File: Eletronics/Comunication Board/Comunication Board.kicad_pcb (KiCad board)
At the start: 2 copper layers, 28 parts, among them K1 RELE, T1 AMS1117/3V3, U1 ESP32-S3-WROOM-1-N8R2, U2 BATERIA, U3 MAX17048G

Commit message: Comunication Board edit
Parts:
- added C10: 1 uF, Capacitor_SMD:C_0603_1608Metric, F.Cu at (158.1, 111.9)
- added C9: 1 uF, Capacitor_SMD:C_0603_1608Metric, F.Cu at (164.6, 102.2)
- added D1: 1N4007, Diode_SMD:D_SMA, F.Cu at (152.1, 110.8)
- added J1: USB, Connector_USB:USB_Micro-B_Amphenol_10118194_Horizontal, F.Cu at (153.0, 104.1)
- added J3: Conn_01x03_Female, Connector_PinSocket_2.54mm:PinSocket_1x03_P2.54mm_Vertical, F.Cu at (160.3, 103.3)
- added R10: 100 Ω, Resistor_SMD:R_0603_1608Metric, F.Cu at (164.6, 107.3)
- added R9: 100 Ω, Resistor_SMD:R_0603_1608Metric, F.Cu at (164.6, 104.7)
- moved BOOT1 6.30 mm to (186.2, 75.9)
- moved C2 6.30 mm to (210.7, 64.8)
- moved C4 6.30 mm to (202.7, 69.9)
- moved C5 6.30 mm to (201.4, 72.5)
- moved C8 6.30 mm to (195.8, 79.0)
- moved EN1 6.30 mm to (196.0, 58.8)
- moved L2 6.30 mm to (193.4, 71.4)
- moved L3 6.30 mm to (193.4, 74.0)
- moved L4 6.30 mm to (202.7, 64.9)
- moved POWER1 6.30 mm to (171.5, 74.9)
- moved R4 6.30 mm to (193.3, 76.5)
- moved R6 6.30 mm to (216.6, 57.0)
- moved R7 6.30 mm to (206.7, 64.8)
- moved R8 6.30 mm to (191.8, 80.1)
- moved U2 6.30 mm to (204.7, 59.2)
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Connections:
- K1 pad NC: GPIO -> GPIO45
- R1 pad 1: GPIO -> GPIO6
- R5 pad 1: GPIO -> GPIO5
- R6 pad 1: GPIO -> GPIO7
- U1 pad 13: unconnected-(U1-Pad13) -> USB_D-
- U1 pad 14: unconnected-(U1-Pad14) -> USB_D+
- U1 pad 18: unconnected-(U1-Pad18) -> SPI_CS
- U1 pad 19: unconnected-(U1-Pad19) -> SPI_MOSI
- U1 pad 20: unconnected-(U1-Pad20) -> SPI_CLK
- U1 pad 21: unconnected-(U1-Pad21) -> SPI_MISO
- U1 pad 26: unconnected-(U1-Pad26) -> GPIO45
- U1 pad 33: unconnected-(U1-Pad33) -> GPIO40
- U1 pad 35: unconnected-(U1-Pad35) -> GPIO42
- U1 pad 36: unconnected-(U1-Pad36) -> RXD0
- U1 pad 37: unconnected-(U1-Pad37) -> TXD0
- U1 pad 5: unconnected-(U1-Pad5) -> GPIO5
- U1 pad 6: unconnected-(U1-Pad6) -> GPIO6
- U1 pad 7: unconnected-(U1-Pad7) -> GPIO7
- U3 pad 5: AnyGPIO -> GPIO40

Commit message: Comunication board
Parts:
- added BZ1: Buzzer, Buzzer_Beeper:Buzzer_12x9.5RM7.6, F.Cu at (135.2, 52.3)
- added H4: MountingHole, SirBoardLibrary:MountingHole_M2.5_SirBoard, F.Cu at (156.9, 48.5)
- added H4: MountingHole, SirBoardLibrary:MountingHole_M2.5_SirBoard, F.Cu at (117.8, 48.5)
- added H4: MountingHole, SirBoardLibrary:MountingHole_M2.5_SirBoard, F.Cu at (156.9, 87.8)
- added H4: MountingHole, SirBoardLibrary:MountingHole_M2.5_SirBoard, F.Cu at (117.6, 87.8)
- added J2: Conn_01x04_Female, Connector_PinSocket_2.54mm:PinSocket_1x04_P2.54mm_Vertical, F.Cu at (139.1, 68.5)
- added J4: Conn_01x03_Female, Connector_PinSocket_2.54mm:PinSocket_1x03_P2.54mm_Vertical, F.Cu at (121.9, 53.4)
- POWER1: footprint Button_Switch_THT:Nidec_Copal_SH-7010C -> Button_Switch_THT:SW_DIP_SPSTx01_Slide_6.7x4.1mm_W7.62mm_P2.54mm_LowProfile
- moved C3 98.1 mm to (116.5, 79.4), turned to 180 degrees
- moved C7 94.6 mm to (121.1, 80.8)
- moved C2 90.8 mm to (121.1, 79.2)
- moved R7 89.9 mm to (117.1, 56.9), turned to 180 degrees
- moved R2 86.9 mm to (121.1, 82.5)
- moved R6 82.5 mm to (136.7, 77.5)
- moved C1 81.5 mm to (116.5, 81.3), turned to 180 degrees
- moved R3 80.5 mm to (122.4, 47.2), turned to 180 degrees
- moved R5 76.8 mm to (136.7, 73.7)
- moved EN1 76.4 mm to (124.7, 86.3)
- moved R8 75.3 mm to (120.2, 56.9)
- moved C8 75.0 mm to (126.7, 49.7), turned to 90 degrees
- moved R1 72.7 mm to (126.7, 56.7)
- moved L1 72.2 mm to (122.3, 49.8)
- moved L4 66.9 mm to (136.7, 75.9)
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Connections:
- net -BAT renamed GND
- J3 pad 2: TXD0 -> RXD0
- J3 pad 3: RXD0 -> TXD0
- K1 pad NC: GPIO45 -> GPIO46
- R1 pad 1: GPIO6 -> GPIO42
- R5 pad 1: GPIO5 -> GPIO9
- R6 pad 1: GPIO7 -> GPIO3
- U1 pad 15: SDA -> GPIO3
- U1 pad 16: unconnected-(U1-Pad16) -> GPIO46
- U1 pad 17: unconnected-(U1-Pad17) -> GPIO9
- U1 pad 27: unconnected-(U1-Pad27) -> I00
- U1 pad 39: unconnected-(U1-Pad39) -> SDA
- U1 pad 5: GPIO5 -> unconnected-(U1-Pad5)
- U1 pad 6: GPIO6 -> unconnected-(U1-Pad6)
- U1 pad 7: GPIO7 -> unconnected-(U1-Pad7)
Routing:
- net GND: track 0.00 -> 68.7 mm, vias 0 -> 10
- net +3.3V: track 0.00 -> 67.1 mm, vias 0 -> 2
- net +BAT: track 0.00 -> 39.4 mm, vias 0 -> 2
- net I00: track 0.00 -> 36.6 mm, vias 0 -> 2
- net SCL: track 0.00 -> 26.6 mm, vias 0 -> 2
- net SDA: track 0.00 -> 25.1 mm
- net EN: track 0.00 -> 16.3 mm
- net Net-(D1-Pad2): track 0.00 -> 14.1 mm
- net GPIO40: track 0.00 -> 11.7 mm
- net SPI_MISO: track 0.00 -> 10.0 mm
- net Net-(C10-Pad1): track 0.00 -> 9.98 mm
- net RXD0: track 0.00 -> 9.72 mm
- net GPIO45: track 0.00 -> 9.69 mm
- net SPI_CLK: track 0.00 -> 9.31 mm
- net TXD0: track 0.00 -> 8.70 mm
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- added copper zone on B.Cu, net +5V
- added copper zone on F.Cu, net +5V
- added copper zone on B.Cu, net GND
- added copper zone on F.Cu, net GND
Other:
- board outline added: 44.6 x 44.5 mm

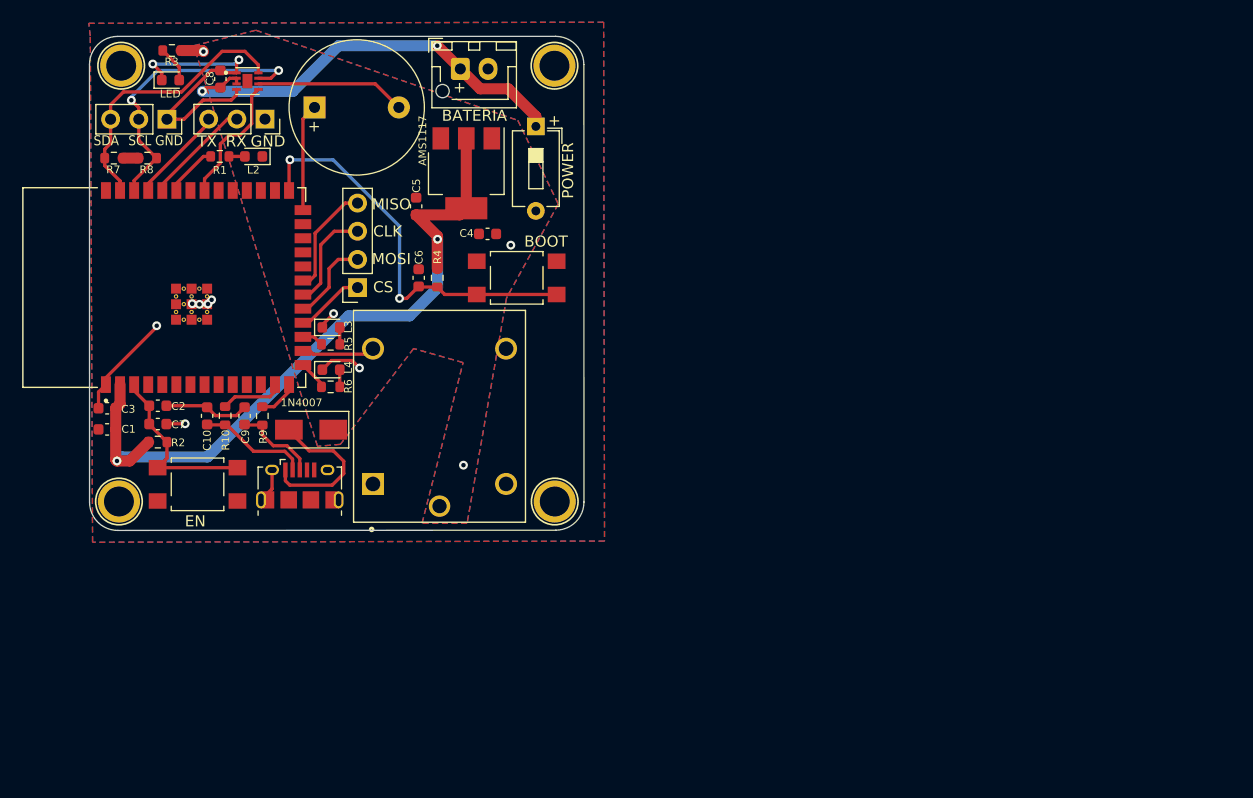
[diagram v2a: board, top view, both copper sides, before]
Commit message: Design Commutication Board pcb
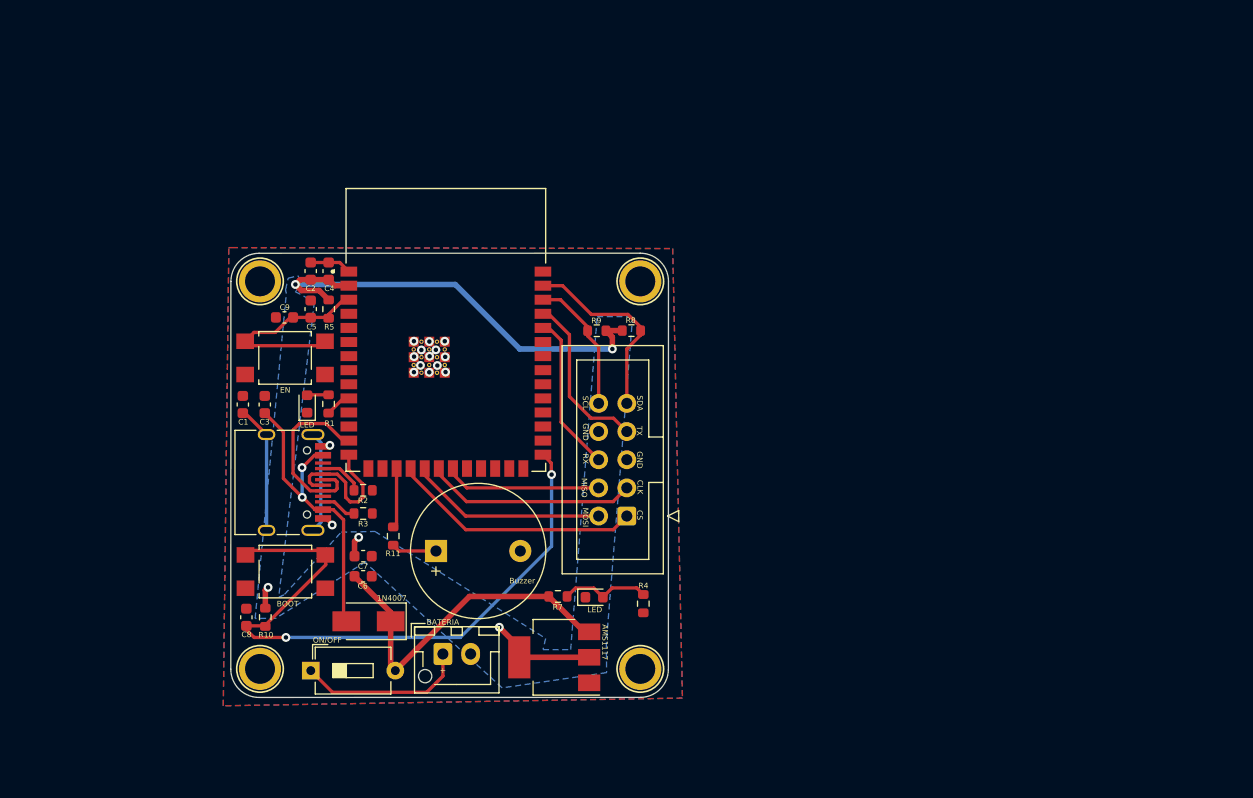
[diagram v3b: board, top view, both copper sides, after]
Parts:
- removed C10: 1 uF, Capacitor_SMD:C_0603_1608Metric
- removed the H4 at (156.9, 48.5)
- removed the H4 at (117.8, 48.5)
- removed the H4 at (156.9, 87.8)
- removed the H4 at (117.6, 87.8)
- removed J3, J4: Conn_01x03_Female, Connector_PinSocket_2.54mm:PinSocket_1x03_P2.54mm_Vertical
- removed K1: RELE, SRD:RELAY_SRD-05VDC-SL-C
- removed L2, L3: LED, LED_SMD:LED_0603_1608Metric
- removed R6: 330 Ω, Resistor_SMD:R_0603_1608Metric
- removed U3: MAX17048G, MAX17048:SON50P200X200X80-9N
- added G: LOGO, Arduino:Logo.Neon, B.Cu at (154.9, 72.6)
- added H4: MountingHole, SirBoardLibrary:MountingHole_M2.5_SirBoard, F.Cu at (130.3, 68.0)
- added H4: MountingHole, SirBoardLibrary:MountingHole_M2.5_SirBoard, F.Cu at (164.6, 68.0)
- added H4: MountingHole, SirBoardLibrary:MountingHole_M2.5_SirBoard, F.Cu at (130.3, 102.9)
- added H4: MountingHole, SirBoardLibrary:MountingHole_M2.5_SirBoard, F.Cu at (164.6, 102.9)
- added R11: 330 Ω, Resistor_SMD:R_0603_1608Metric, F.Cu at (142.3, 90.9)
- C2, C9: value 1 uF -> 100 nF
- C3: value 10 uF -> 100 nF
- C5: value 10 uF -> 1 uF
- C6, C7: value 100 nF -> 10 uF
- J1: value USB -> USB_C_Receptacle_USB2.0; footprint Connector_USB:USB_Micro-B_Amphenol_10118194_Horizontal -> c:USB_C_Receptacle_HRO_TYPE-C-31-M-12
- J2: value Conn_01x04_Female -> Conn_01x10_Female; footprint Connector_PinSocket_2.54mm:PinSocket_1x04_P2.54mm_Vertical -> Connector_IDC:IDC-Header_2x05_P2.54mm_Vertical
- R10: value 100 Ω -> 10K
- R2: value 10K -> 5.1k
- R3: value 330 Ω -> 5.1k
- R4: value 10K -> 1.5 KΩ
- R5: value 330 Ω -> 10K
- R7: value 4K7 -> 330 Ω
- R9: value 100 Ω -> 4K7
- U1: value ESP32-S3-WROOM-1-N8R2 -> BATERIA; footprint lib:XCVR_ESP32-S3-WROOM-1-N8R2 -> Connector_JST:JST_XH_B2B-XH-AM_1x02_P2.50mm_Vertical
- U2: value BATERIA -> ESP32-S3-WROOM-1-N8R2; footprint Connector_JST:JST_XH_B2B-XH-AM_1x02_P2.50mm_Vertical -> lib:XCVR_ESP32-S3-WROOM-1-N8R2
- moved R7 56.3 mm to (157.2, 96.4), turned to 0 degrees
- moved POWER1 53.1 mm to (134.9, 103.1), turned to 0 degrees
- moved C8 48.6 mm to (129.1, 98.3)
- moved R8 46.3 mm to (163.8, 72.4)
- moved R3 45.2 mm to (139.6, 88.9), turned to 0 degrees
- moved T1 44.4 mm to (156.9, 101.9), turned to 180 degrees
- moved U1 41.5 mm to (146.8, 101.6), turned to 0 degrees
- moved BZ1 41.5 mm to (146.2, 92.3)
- moved R4 34.8 mm to (164.9, 97.0)
- moved BOOT1 33.7 mm to (132.6, 94.2), turned to 0 degrees
- moved J2 31.8 mm to (163.4, 89.1)
- moved L1 31.7 mm to (134.6, 79.0), turned to 90 degrees
- moved L4 31.4 mm to (160.5, 96.5)
- moved R9 31.1 mm to (160.7, 72.4), turned to 180 degrees
- moved C6 27.4 mm to (139.6, 94.6), turned to 0 degrees
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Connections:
- BOOT1 pad 2: GND -> GNDREF
- BZ1 pad 1: GPIO45 -> Net-(BZ1-Pad1)
- BZ1 pad 2: GND -> GNDREF
- C1 pad 1: +3.3V -> Net-(C1-Pad1)
- C1 pad 2: GND -> GNDREF
- C2 pad 1: EN -> +3.3V
- C2 pad 2: GND -> GNDREF
- C3 pad 1: +3.3V -> Net-(C3-Pad1)
- C3 pad 2: GND -> GNDREF
- C4 pad 1: +5V -> +3.3V
- C4 pad 2: GND -> GNDREF
- C5 pad 1: +3.3V -> EN
- C5 pad 2: GND -> GNDREF
- C6 pad 1: I00 -> +5V
- C6 pad 2: GND -> GNDREF
- C7 pad 1: EN -> +3.3V
- C7 pad 2: GND -> GNDREF
- C8 pad 1: +BAT -> I00
- C8 pad 2: GND -> GNDREF
- C9 pad 1: Net-(C9-Pad1) -> EN
- C9 pad 2: GND -> GNDREF
- D1 pad 2: Net-(D1-Pad2) -> Net-(C3-Pad1)
- EN1 pad 2: GND -> GNDREF
- L1 pad 1: GND -> GNDREF
- L4 pad 1: GND -> GNDREF
- POWER1 pad 1: +BAT -> Net-(POWER1-Pad1)
- R1 pad 1: GPIO42 -> GPIO17
- R1 pad 2: Net-(L2-Pad2) -> Net-(L1-Pad2)
- R10 pad 1: USB_D- -> +3.3V
- R10 pad 2: Net-(C10-Pad1) -> I00
- R2 pad 1: +3.3V -> Net-(J1-PadA5)
- R2 pad 2: EN -> GNDREF
- R3 pad 1: +5V -> Net-(J1-PadB5)
- R3 pad 2: Net-(L1-Pad2) -> GNDREF
- R4 pad 1: +3.3V -> Net-(L4-Pad2)
- R4 pad 2: I00 -> GNDREF
- R5 pad 1: GPIO9 -> +3.3V
- R5 pad 2: Net-(L3-Pad2) -> EN
- R7 pad 1: 3V3 -> +5V
- R7 pad 2: SDA -> Net-(L4-Pad2)
- R8 pad 1: 3V3 -> +3.3V
- R8 pad 2: SCL -> SDA
- R9 pad 1: USB_D+ -> +3.3V
- R9 pad 2: Net-(C9-Pad1) -> SCL
- T1 pad 1: GND -> GNDREF
- U1 pad 1: GND -> Net-(POWER1-Pad1)
- U1 pad 2: +3.3V -> GNDREF
- U2 pad 1: +BAT -> GNDREF
- U2 pad 2: GND -> +3.3V
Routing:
- net GND: track 68.7 -> 0.00 mm, vias 10 -> 0
- net +BAT: track 39.4 -> 0.00 mm, vias 2 -> 0
- net +5V: track 2.06 -> 31.6 mm, vias 3 -> 0
- net Net-(C3-Pad1): track 0.00 -> 28.6 mm, vias 0 -> 2
- net I00: track 36.6 -> 58.0 mm
- net Net-(C1-Pad1): track 0.00 -> 20.8 mm
- net SPI_CS: track 6.24 -> 22.6 mm
- net Net-(POWER1-Pad1): track 0.00 -> 15.3 mm
- net SCL: track 26.6 -> 12.4 mm, vias 2 -> 0
- net Net-(D1-Pad2): track 14.1 -> 0.00 mm
- net GPIO40: track 11.7 -> 0.00 mm
- net USB_D-: track 5.68 -> 16.5 mm
- net +3.3V: track 67.1 -> 56.7 mm, vias 2 -> 5
- net SPI_MOSI: track 7.76 -> 17.8 mm
- net Net-(C10-Pad1): track 9.98 -> 0.00 mm
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- added copper zone on B.Cu, net +3.3V
- added copper zone on B.Cu, net GNDREF
- added copper zone on F.Cu, net GNDREF
- removed copper zone on B.Cu, net +5V
- removed copper zone on F.Cu, net +5V
- removed copper zone on B.Cu, net GND
- removed copper zone on F.Cu, net GND
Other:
- board size 44.6 x 44.5 mm -> 39.5 x 40.1 mm
- board text added: "Project NEON"
- board text added: "SSL V1"
